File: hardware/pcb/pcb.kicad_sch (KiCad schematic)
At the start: 32 parts, among them J1 L_GPIO, J2 R_GPIO, J3 USB_C_Receptacle_USB2.0_14P, U1 ESP32-C3-WROOM-02, U3 TPS62291

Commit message: PCB: add some silkscreen art and transparency edits
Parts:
- D1: now not fitted
- R12: value R -> 100; LCSC Part (none) -> C106232
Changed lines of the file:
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@@
 		(in_bom yes)
 		(on_board yes)
-		(dnp no)
+		(dnp yes)
 		(fields_autoplaced yes)
 		(property "Reference" "D1"
@@
 			)
 		)
-		(property "Value" "R"
+		(property "Value" "100"
 			(at 123.19 123.19 90)
 			(effects
@@
 			(effects
 				(font
+					(size 1.27 1.27)
+				)
+				(hide yes)
+			)
+		)
+		(property "LCSC Part" "C106232"
+			(at 123.19 127 90)
+			(effects
+				(font

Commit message: PCB: modified LCSC part numbers for D5 and J3
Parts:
- D5: LCSC Part C114586 -> C2761795
- J3: LCSC Part C5362630 -> C2988369
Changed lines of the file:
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@@
 			)
 		)
-		(property "LCSC Part" "C5362630"
+		(property "LCSC Part" "C2988369"
 			(at 33.02 157.48 0)
 			(effects
@@
 			)
 		)
-		(property "LCSC Part" "C114586"
+		(property "LCSC Part" "C2761795"
 			(at 157.48 127 0)
 			(effects

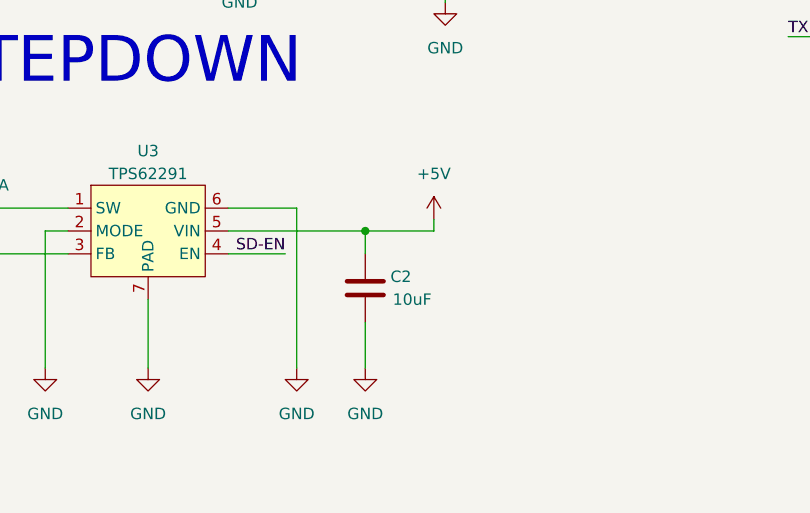
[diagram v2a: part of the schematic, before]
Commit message: Added that small bitchass resistor that was missing. (For those who come after)
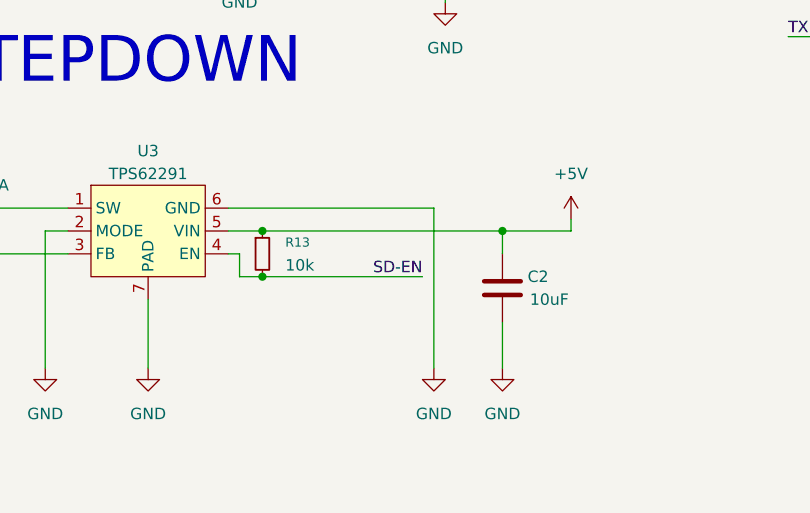
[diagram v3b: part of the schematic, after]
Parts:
- added R13: 10k, symbol Device:R_Small
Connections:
- net +5V: now also R13.1
- net SD-EN: now also R13.2
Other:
- moved on the sheet: C2
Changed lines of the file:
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@@
 	)
 	(junction
-		(at 148.59 162.56)
+		(at 163.83 162.56)
 		(diameter 0)
 		(color 0 0 0 0)
@@
 	)
 	(junction
+		(at 137.16 162.56)
+		(diameter 0)
+		(color 0 0 0 0)
+	)
+	(junction
+		(at 137.16 167.64)
+		(diameter 0)
+		(color 0 0 0 0)
+	)
+	(junction
 		(at 97.79 165.1)
 		(diameter 0)
@@
 	(wire
 		(pts
+			(xy 134.62 167.64) (xy 134.62 165.1)
+		)
+		(stroke
+			(width 0)
+			(type default)
+		)
+	)
+	(wire
+		(pts
 			(xy 139.7 45.72) (xy 156.21 45.72)
 		)
@@
 	(wire
 		(pts
-			(xy 156.21 161.29) (xy 156.21 162.56)
+			(xy 171.45 161.29) (xy 171.45 162.56)
 		)
 		(stroke
@@
 	(wire
 		(pts
+			(xy 137.16 162.56) (xy 163.83 162.56)
+		)
+		(stroke
+			(width 0)
+			(type default)
+		)
+	)
+	(wire
+		(pts
 			(xy 246.38 153.67) (xy 246.38 157.48)
 		)
@@
 	(wire
 		(pts
-			(xy 140.97 160.02) (xy 133.35 160.02)
+			(xy 156.21 160.02) (xy 133.35 160.02)
 		)
 		(stroke
@@
 	(wire
 		(pts
-			(xy 148.59 165.1) (xy 148.59 162.56)
+			(xy 163.83 165.1) (xy 163.83 162.56)
 		)
 		(stroke
@@
 	(wire
 		(pts
-			(xy 156.21 162.56) (xy 148.59 162.56)
+			(xy 137.16 167.64) (xy 154.94 167.64)
+		)
+		(stroke
+			(width 0)
+			(type default)
+		)
+	)
+	(wire
+		(pts
+			(xy 171.45 162.56) (xy 163.83 162.56)
 		)
 		(stroke
@@
 	(wire
 		(pts
+			(xy 134.62 165.1) (xy 133.35 165.1)
+		)
+		(stroke
+			(width 0)
+			(type default)
+		)
+	)
+	(wire
+		(pts
 			(xy 219.71 140.97) (xy 224.79 140.97)
 		)
@@
 	(wire
 		(pts
-			(xy 140.97 177.8) (xy 140.97 160.02)
+			(xy 156.21 177.8) (xy 156.21 160.02)
 		)
 		(stroke
@@
 	(wire
 		(pts
-			(xy 133.35 165.1) (xy 139.7 165.1)
-		)
-		(stroke
-			(width 0)
-			(type default)
-		)
-	)
-	(wire
-		(pts
-			(xy 133.35 162.56) (xy 148.59 162.56)
+			(xy 133.35 162.56) (xy 137.16 162.56)
 		)
 		(stroke
@@
 	(wire
 		(pts
-			(xy 148.59 177.8) (xy 148.59 172.72)
+			(xy 163.83 177.8) (xy 163.83 172.72)
 		)
 		(stroke
@@
 	(wire
 		(pts
+			(xy 134.62 167.64) (xy 137.16 167.64)
+		)
+		(stroke
+			(width 0)
+			(type default)
+		)
+	)
+	(wire
+		(pts
 			(xy 134.62 41.91) (xy 134.62 43.18)
 		)
@@
 	)
 	(label "SD-EN"
-		(at 139.7 165.1 180)
+		(at 154.94 167.64 180)
 		(effects
 			(font
@@
 	)
 	(symbol
+		(lib_name "R_Small_2")
+		(lib_id "Device:R_Small")
+		(at 137.16 165.1 0)
+		(unit 1)
+		(exclude_from_sim no)
+		(in_bom yes)
+		(on_board yes)
+		(dnp no)
+		(fields_autoplaced yes)
+		(property "Reference" "R13"
+			(at 139.7 163.8299 0)
+			(effects
+				(font
+					(size 1.016 1.016)
+				)
+				(justify left)
+			)
+		)
+		(property "Value" "10k"
+			(at 139.7 166.3699 0)
+			(effects
+				(font
+					(size 1.27 1.27)
+				)
+				(justify left)
+			)
+		)
+		(property "Footprint" ""
+			(at 137.16 165.1 0)
+			(effects
+				(font
+					(size 1.27 1.27)
+				)
+				(hide yes)
+			)
+		)
+		(property "Datasheet" "~"
+			(at 137.16 165.1 0)
+			(effects
+				(font
+					(size 1.27 1.27)
+				)
+				(hide yes)
+			)
+		)
+		(property "Description" "Resistor, small symbol"
+			(at 137.16 165.1 0)
+			(effects
+				(font
+					(size 1.27 1.27)
+				)
+				(hide yes)
+			)
+		)
+		(pin "2"
+		)
+		(pin "1"
+		)
+		(instances
+			(project ""
+				(path "/9dc8e51d-ce6f-43bb-9eca-8a5aff8e2cbe"
+					(reference "R13")
+					(unit 1)
+				)
+			)
+		)
+	)
+	(symbol
 		(lib_id "Device:D_Schottky_Small")
 		(at 64.77 142.24 180)
@@
 	(symbol
 		(lib_id "power:+5V")
-		(at 156.21 161.29 0)
+		(at 171.45 161.29 0)
 		(unit 1)
 		(exclude_from_sim no)
@@
 		(fields_autoplaced yes)
 		(property "Reference" "#PWR012"
-			(at 156.21 165.1 0)
+			(at 171.45 165.1 0)
 			(effects
 				(font
@@
 		)
 		(property "Value" "+5V"
-			(at 156.21 156.21 0)
+			(at 171.45 156.21 0)
 			(effects
 				(font
@@
 		)
 		(property "Footprint" ""
-			(at 156.21 161.29 0)
+			(at 171.45 161.29 0)
 			(effects
 				(font
@@
 		)
 		(property "Datasheet" ""
-			(at 156.21 161.29 0)
+			(at 171.45 161.29 0)
 			(effects
 				(font
@@
 		)
 		(property "Description" "Power symbol creates a global label with name \"+5V\""
-			(at 156.21 161.29 0)
+			(at 171.45 161.29 0)
 			(effects
 				(font
@@
 	(symbol
 		(lib_id "Device:C")
-		(at 148.59 168.91 0)
+		(at 163.83 168.91 0)
 		(unit 1)
 		(exclude_from_sim no)
@@
 		(dnp no)
 		(property "Reference" "C2"
-			(at 151.384 167.64 0)
+			(at 166.624 167.64 0)
 			(effects
 				(font
@@
 		)
 		(property "Value" "10uF"
-			(at 151.638 170.18 0)
+			(at 166.878 170.18 0)
 			(effects
 				(font
@@
 		)
 		(property "Footprint" "Capacitor_SMD:C_0402_1005Metric"
-			(at 149.5552 172.72 0)
+			(at 164.7952 172.72 0)
 			(effects
 				(font
@@
 		)
 		(property "Datasheet" "~"
-			(at 148.59 168.91 0)
+			(at 163.83 168.91 0)
 			(effects
 				(font
@@
 		)
 		(property "Description" "Unpolarized capacitor"
-			(at 148.59 168.91 0)
+			(at 163.83 168.91 0)
 			(effects
 				(font
@@
 		)
 		(property "Description_1" ""
-			(at 148.59 168.91 0)
+			(at 163.83 168.91 0)
 			(effects
 				(font
@@
 		)
 		(property "LCSC Part" "C315248"
-			(at 148.59 168.91 0)
+			(at 163.83 168.91 0)
 			(effects
 				(font
@@
 		)
 		(property "Shop link" "https://www.lcsc.com/product-detail/C315248.html?s_z=n_C%25200402%252010%2520uf"
-			(at 148.59 168.91 0)
+			(at 163.83 168.91 0)
 			(effects
 				(font
@@
 	(symbol
 		(lib_id "power:GND")
-		(at 140.97 177.8 0)
+		(at 156.21 177.8 0)
 		(mirror y)
 		(unit 1)
@@
 		(fields_autoplaced yes)
 		(property "Reference" "#PWR035"
-			(at 140.97 184.15 0)
+			(at 156.21 184.15 0)
 			(effects
 				(font
@@
 		)
 		(property "Value" "GND"
-			(at 140.97 182.88 0)
+			(at 156.21 182.88 0)
 			(effects
 				(font
@@
 		)
 		(property "Footprint" ""
-			(at 140.97 177.8 0)
+			(at 156.21 177.8 0)
 			(effects
 				(font
@@
 		)
 		(property "Datasheet" ""
-			(at 140.97 177.8 0)
+			(at 156.21 177.8 0)
 			(effects
 				(font
@@
 		)
 		(property "Description" "Power symbol creates a global label with name \"GND\" , ground"
-			(at 140.97 177.8 0)
+			(at 156.21 177.8 0)
 			(effects
 				(font
@@
 	(symbol
 		(lib_id "power:GND")
-		(at 148.59 177.8 0)
+		(at 163.83 177.8 0)
 		(mirror y)
 		(unit 1)
@@
 		(fields_autoplaced yes)
 		(property "Reference" "#PWR036"
-			(at 148.59 184.15 0)
+			(at 163.83 184.15 0)
 			(effects
 				(font
@@
 		)
 		(property "Value" "GND"
-			(at 148.59 182.88 0)
+			(at 163.83 182.88 0)
 			(effects
 				(font
@@
 		)
 		(property "Footprint" ""
-			(at 148.59 177.8 0)
+			(at 163.83 177.8 0)
 			(effects
 				(font
@@
 		)
 		(property "Datasheet" ""
-			(at 148.59 177.8 0)
+			(at 163.83 177.8 0)
 			(effects
 				(font
@@
 		)
 		(property "Description" "Power symbol creates a global label with name \"GND\" , ground"
-			(at 148.59 177.8 0)
+			(at 163.83 177.8 0)
 			(effects
 				(font

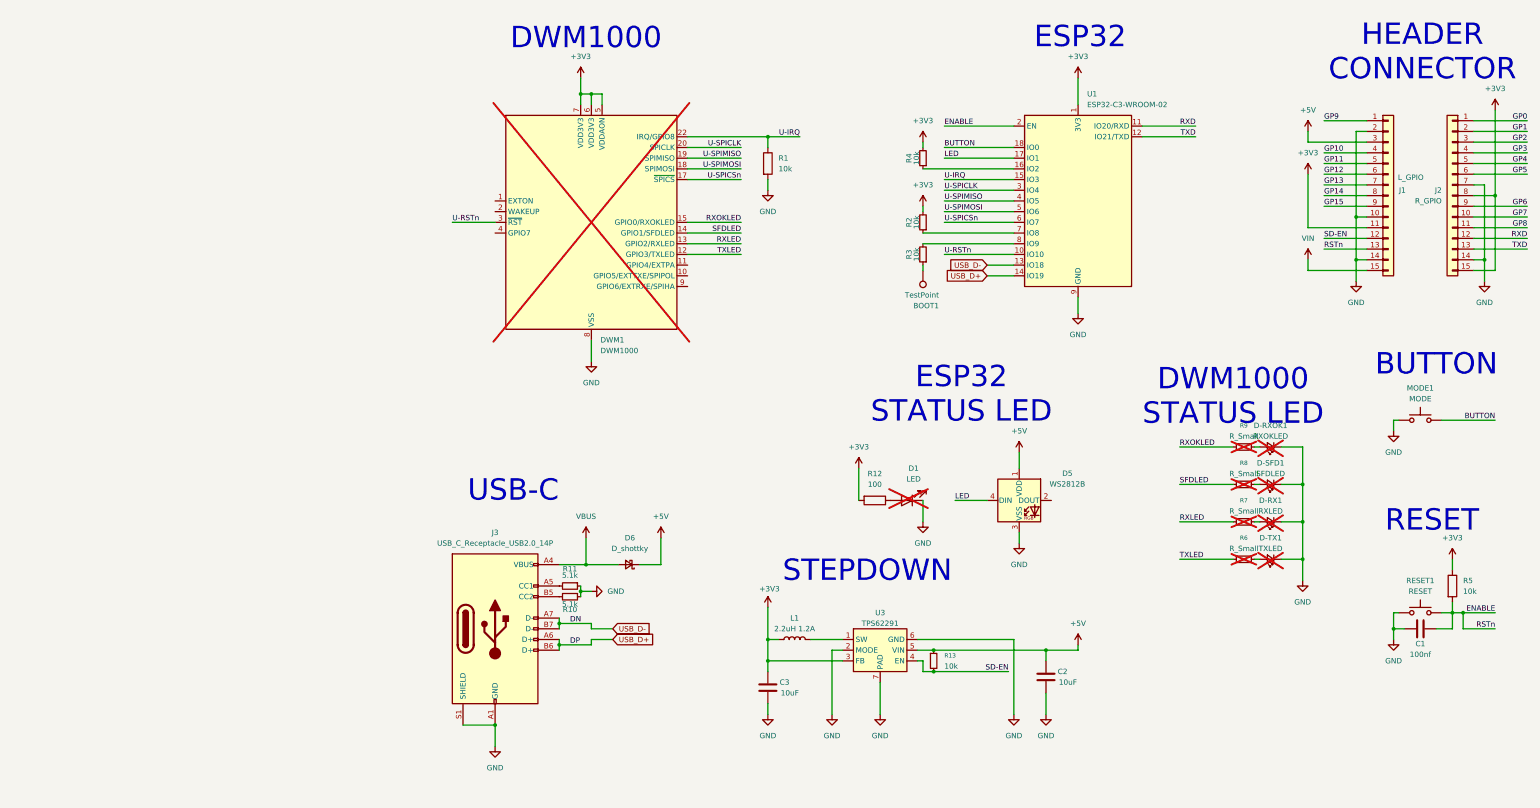
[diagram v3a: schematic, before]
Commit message: DWM3000 schematic done
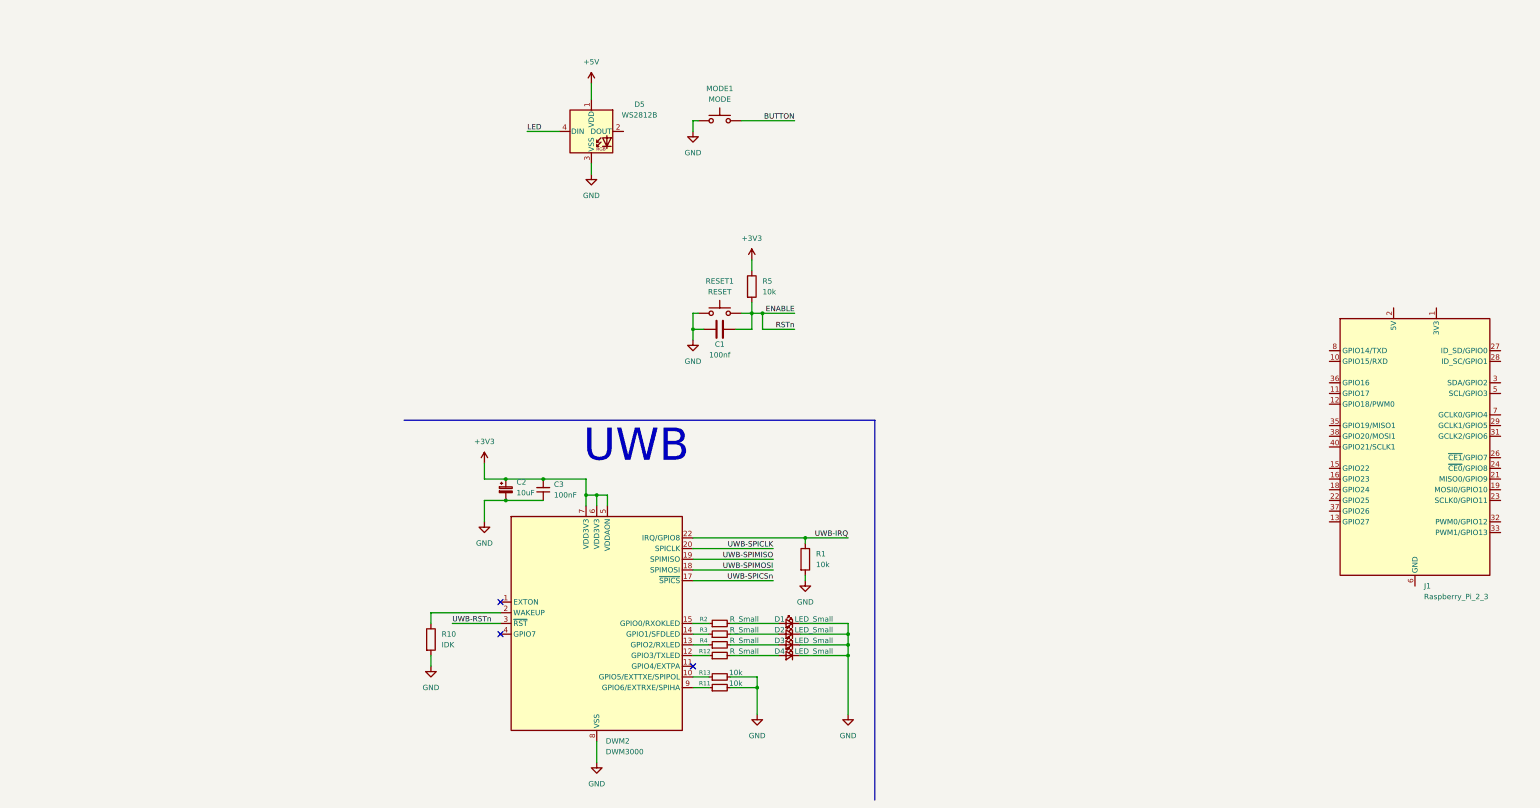
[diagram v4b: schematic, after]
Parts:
- removed BOOT1: TestPoint, TestPoint:TestPoint_Pad_D1.5mm, symbol Connector:TestPoint
- removed C2, C3: 10uF, Capacitor_SMD:C_0402_1005Metric, symbol Device:C
- removed D-RX1: RXLED, LED_SMD:LED_0402_1005Metric_Pad0.77x0.64mm_HandSolder, symbol Device:LED_Small
- removed D-RXOK1: RXOKLED, LED_SMD:LED_0402_1005Metric_Pad0.77x0.64mm_HandSolder, symbol Device:LED_Small
- removed D-SFD1: SFDLED, LED_SMD:LED_0402_1005Metric_Pad0.77x0.64mm_HandSolder, symbol Device:LED_Small
- removed D-TX1: TXLED, LED_SMD:LED_0402_1005Metric_Pad0.77x0.64mm_HandSolder, symbol Device:LED_Small
- removed D1: LED, LED_SMD:LED_0201_0603Metric_Pad0.64x0.40mm_HandSolder, symbol Device:LED
- removed D6: D_shottky, Diode_SMD:D_SOD-123, symbol Device:D_Schottky_Small
- removed DWM1: DWM1000, RF_Module:DWM1000, symbol RF_Module:DWM1000
- removed J1: L_GPIO, Connector_PinHeader_2.54mm:PinHeader_1x15_P2.54mm_Vertical, symbol Connector_Generic:Conn_01x15
- removed J2: R_GPIO, Connector_PinHeader_2.54mm:PinHeader_1x15_P2.54mm_Vertical, symbol Connector_Generic:Conn_01x15
- removed J3: USB_C_Receptacle_USB2.0_14P, Connector_USB:USB_C_Receptacle_G-Switch_GT-USB-7010ASV, symbol Connector:USB_C_Receptacle_USB2.0_14P
- removed L1: 2.2uH 1.2A, Inductor_SMD:L_0805_2012Metric, symbol Device:L
- removed R10: 5.1k, Resistor_SMD:R_0402_1005Metric, symbol Device:R_Small
- removed R12: 100, Resistor_SMD:R_0402_1005Metric, symbol Device:R
- removed R6, R7, R8, R9: R_Small, Resistor_SMD:R_0402_1005Metric_Pad0.72x0.64mm_HandSolder, symbol Device:R_Small
- removed U1: ESP32-C3-WROOM-02, RF_Module:ESP32-C3-WROOM-02, symbol RF_Module:ESP32-C3-WROOM-02
- removed U3: TPS62291, Package_SON:WSON-6-1EP_2x2mm_P0.65mm_EP1x1.6mm_ThermalVias, symbol Sisyphus:TPS62293
- added C2: 10uF, symbol Device:C_Polarized_Small
- added C3: 100nF, symbol Device:C_Small
- added D1, D2, D3, D4: LED_Small, symbol Device:LED_Small
- added DWM2: DWM3000, RF_Module:DWM1000, symbol RF_Module:DWM3000
- added J1: Raspberry_Pi_2_3, Module:RaspberryPi_Pico_Common_Unspecified, symbol Connector:Raspberry_Pi_2_3
- added R10: IDK, Resistor_SMD:R_0402_1005Metric, symbol Device:R
- added R12: R_Small, symbol Device:R_Small
- R11: value 5.1k -> 10k; footprint Resistor_SMD:R_0402_1005Metric -> (none); LCSC Part C2791532 -> (none); Shop link https://www.lcsc.com/product-detail/C413002.html?s_z=n_R%25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 -> (none)
- R2, R3, R4: value 10k -> R_Small; footprint Resistor_SMD:R_0402_1005Metric -> (none); LCSC Part C2936656 -> (none); Shop link https://www.lcsc.com/product-detail/C2936656.html?s_z=n_R%2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 -> (none)
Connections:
- net SD-EN is gone; now on net GND: R13.2
- net +3V3: now also C2.1, C3.2, DWM2.5 (VDDAON), DWM2.6 (VDD3V3), DWM2.7 (VDD3V3); no longer R2.2, R4.2
- net +5V: no longer R13.1
- net GND: now also R11.2, C2.2, C3.1, D1.1 (K), D2.1 (K), D3.1 (K), D4.1 (K), DWM2.16 (VSS), DWM2.21 (VSS), DWM2.23 (VSS), DWM2.24 (VSS), DWM2.8 (VSS), R10.2; no longer R11.1
- net at R2.1: now also DWM2.15 (GPIO0/RXOKLED)
- net at R3.1: now also DWM2.14 (GPIO1/SFDLED)
- net at R4.1: now also DWM2.13 (GPIO2/RXLED)
- net at R3.2: now also D2.2 (A)
- net U-IRQ renamed UWB-IRQ
- net UWB-IRQ: now also DWM2.22 (IRQ/GPIO8)
- new net: J1.1 (3V3), J1.17 (3V3)
- new net: J1.14 (GND), J1.20 (GND), J1.25 (GND), J1.30 (GND), J1.34 (GND), J1.39 (GND), J1.6 (GND), J1.9 (GND)
- new net: J1.2 (5V), J1.4 (5V)
- new net: DWM2.2 (WAKEUP), R10.1
- new net: D1.2 (A), R2.2
- new net: DWM2.10 (GPIO5/EXTTXE/SPIPOL), R13.1
- new net: DWM2.12 (GPIO3/TXLED), R12.1
- new net: DWM2.9 (GPIO6/EXTRXE/SPIHA), R11.1
- new net: D4.2 (A), R12.2
- new net: D3.2 (A), R4.2
- new net UWB-RSTn: DWM2.3 (~{RST})
- new net UWB-SPICLK: DWM2.20 (SPICLK)
- new net UWB-SPICSn: DWM2.17 (~{SPICS})
- new net UWB-SPIMISO: DWM2.19 (SPIMISO)
- new net UWB-SPIMOSI: DWM2.18 (SPIMOSI)
- no-connect marks 0 -> 3
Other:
- note added: "UWB"
- note removed: "BUTTON"
- note removed: "DWM1000"
- note removed: "DWM1000 STATUS LED"
- note removed: "ESP32"
- note removed: "ESP32 STATUS LED"
- note removed: "HEADER CONNECTOR"
- note removed: "RESET"
- note removed: "STEPDOWN"
- note removed: "USB-C"
- moved on the sheet: C1, D5, MODE1, R1, R5, RESET1

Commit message: Added IMU
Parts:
- removed J1: Raspberry_Pi_2_3, Module:RaspberryPi_Pico_Common_Unspecified, symbol Connector:Raspberry_Pi_2_3
- added A1: RaspberryPi_Pico_W, Module:RaspberryPi_Pico_Common_Unspecified, symbol MCU_Module:RaspberryPi_Pico_W
- added C4: 1uF, symbol Device:C_Small
- added C5: 120nF, symbol Device:C_Small
- added C6: 100nF, symbol Device:C_Small
- added FB1: FerriteBead_Small, symbol Device:FerriteBead_Small
- added R6, R7: 10k, symbol Device:R_Small
- added U1: BNO055, Package_LGA:LGA-28_5.2x3.8mm_P0.5mm, symbol Sensor_Motion:BNO055
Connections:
- net +3V3: now also C5.2, C6.1, FB1.1, R6.1, R7.1, U1.28 (VDDIO), U1.3 (VDD); no longer C2.1, C3.2, DWM2.5 (VDDAON), DWM2.6 (VDD3V3), DWM2.7 (VDD3V3)
- net GND: now also C4.2, C5.1, C6.2, U1.18 (COM2), U1.2 (GND), U1.25 (GNDIO), U1.5 (PS1), U1.6 (PS0)
- new net: C2.1, C3.2, DWM2.5 (VDDAON), DWM2.6 (VDD3V3), DWM2.7 (VDD3V3), FB1.2
- new net: C4.1, U1.9 (CAP)
- new net: A1.13 (GND), A1.18 (GND), A1.23 (GND), A1.28 (GND), A1.3 (GND), A1.38 (GND), A1.8 (GND)
- new net IMU-BL_IND: U1.10 (BL_IND)
- new net IMU-I2C_ADDR_SEL: U1.17 (COM3)
- new net IMU-INT: U1.14 (INT)
- new net IMU-SCL: U1.19 (COM1)
- new net IMU-SDA: U1.20 (COM0)
- new net IMU-nBOOT_LOAD_PIN: R6.2, U1.4 (~{BOOT_LOAD_PIN})
- new net IMU-nRESET: R7.2, U1.11 (~{RESET})
- no-connect marks 3 -> 5
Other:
- note added: "IMU"
- moved on the sheet: C1, C2, C3, D5, MODE1, R5, RESET1

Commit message: progress :)
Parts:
- added C7, C8: 100nF, symbol Device:C_Small
- added R8, R9: 4k7, symbol Device:R_Small
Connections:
- net +3V3: now also FB1.2, R8.1, R9.1; no longer FB1.1
- net GND: now also C7.1, C8.1
- net IMU-SCL: now also R9.2
- net IMU-SDA: now also R8.2
- net at C2.1, C3.2, DWM2.5 (VDDAON)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: now also FB1.1, C7.2, C8.2; no longer FB1.2
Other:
- note added: "(T_T)"
- moved on the sheet: C2, C3, FB1
